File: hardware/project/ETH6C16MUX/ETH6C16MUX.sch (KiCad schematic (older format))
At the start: 2 parts

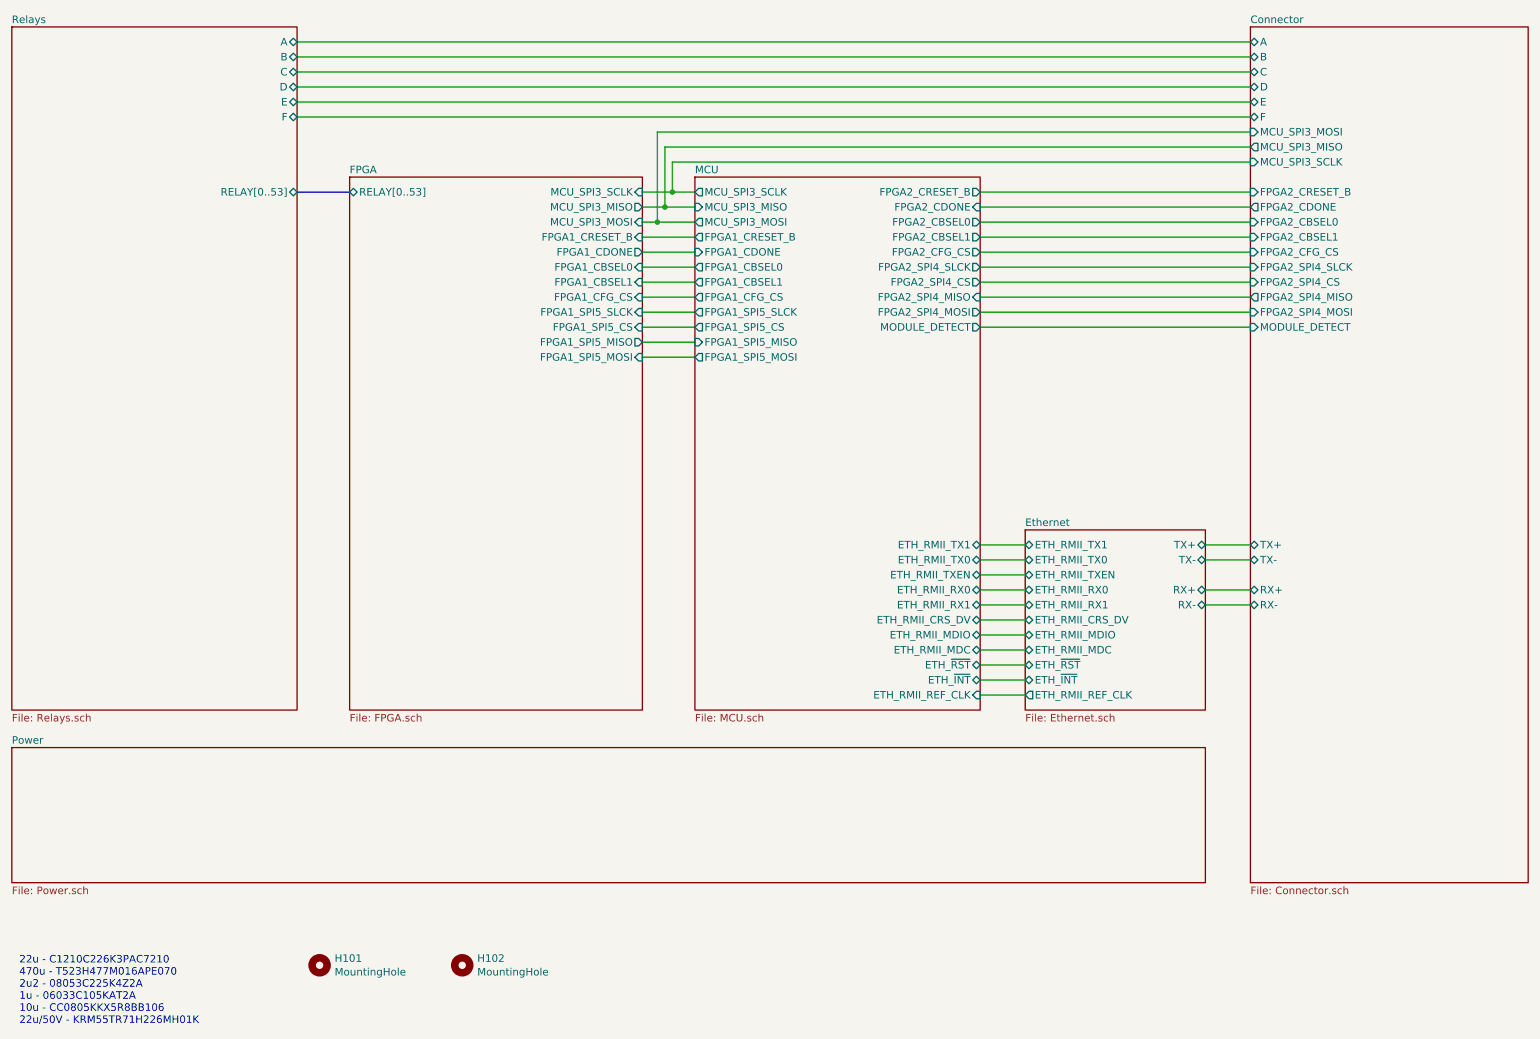
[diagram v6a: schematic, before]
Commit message: Deleted FPGA part and change it for SPI IO chips. Change power supply circuit.
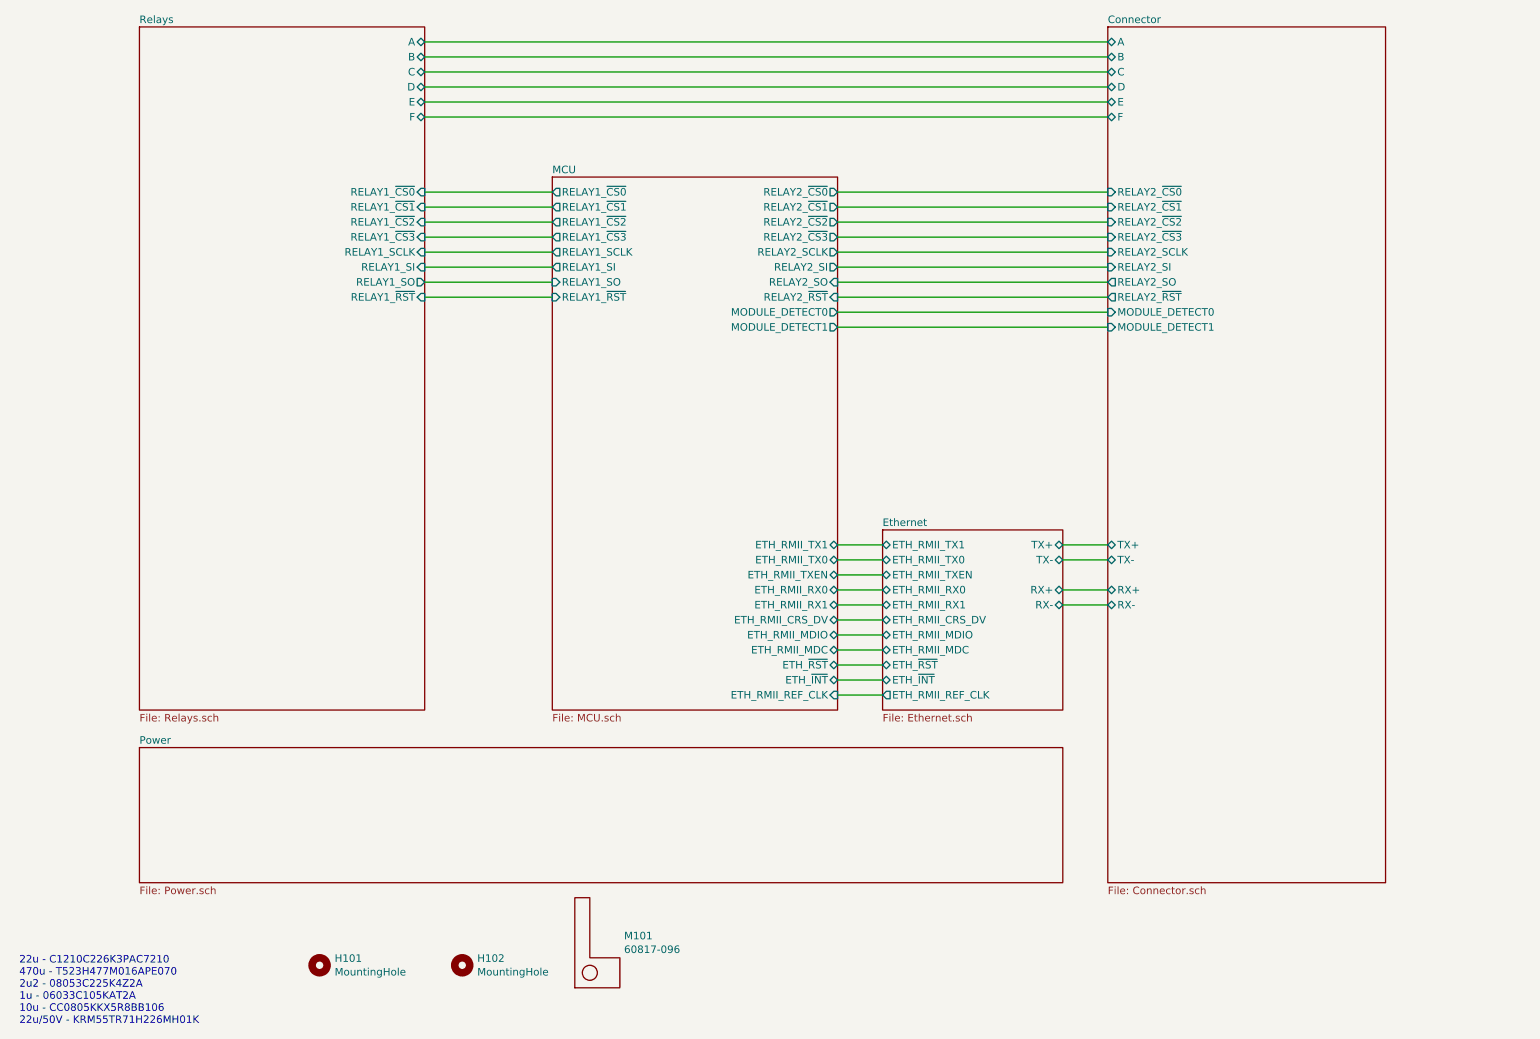
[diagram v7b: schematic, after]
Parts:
- added M101: 60817-096, ETH6C16MXU:60817-096, symbol ETH6C16MUX:60817-096
